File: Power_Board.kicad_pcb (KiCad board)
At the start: 2 copper layers, 48.3 x 24.1 mm, 7 parts, among them J1 Input Power (12 V), J2 Output Power (5V), SW1 SW_SPST, U1 NSR003A0X

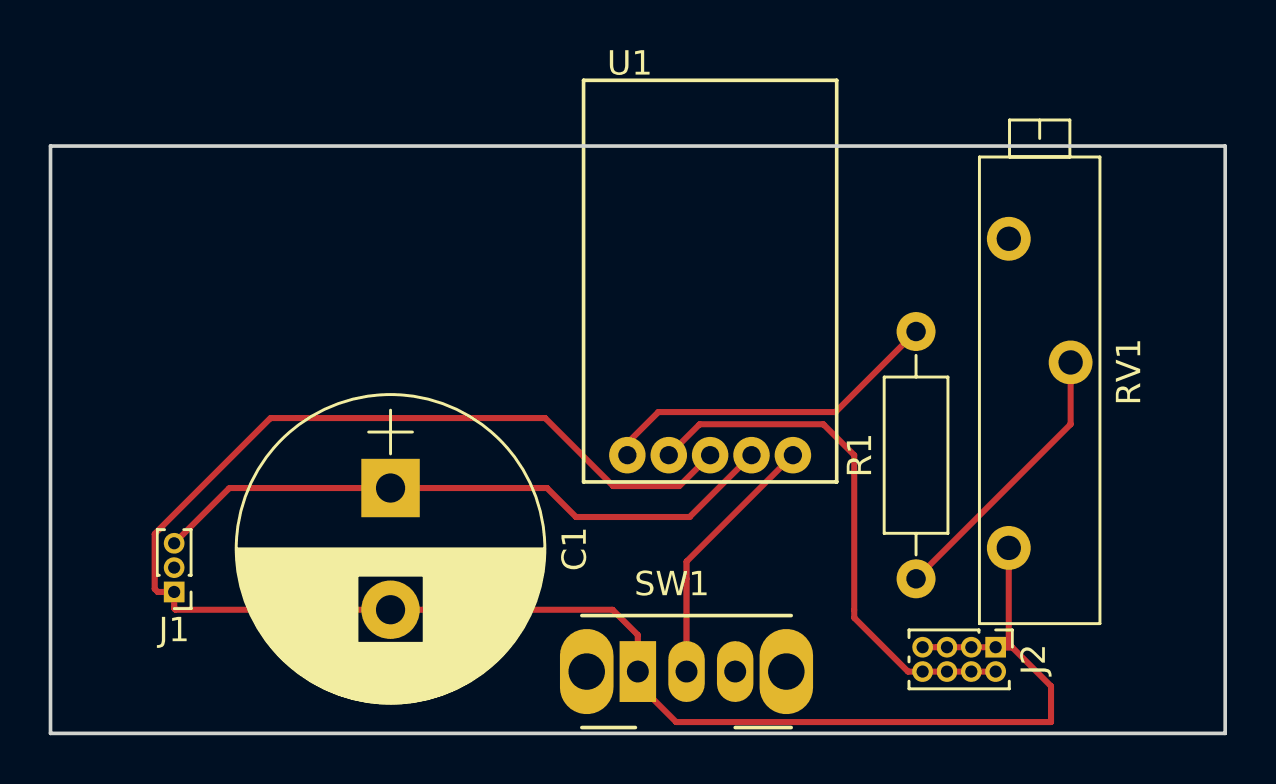
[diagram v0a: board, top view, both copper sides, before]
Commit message: Updated design, added backplane
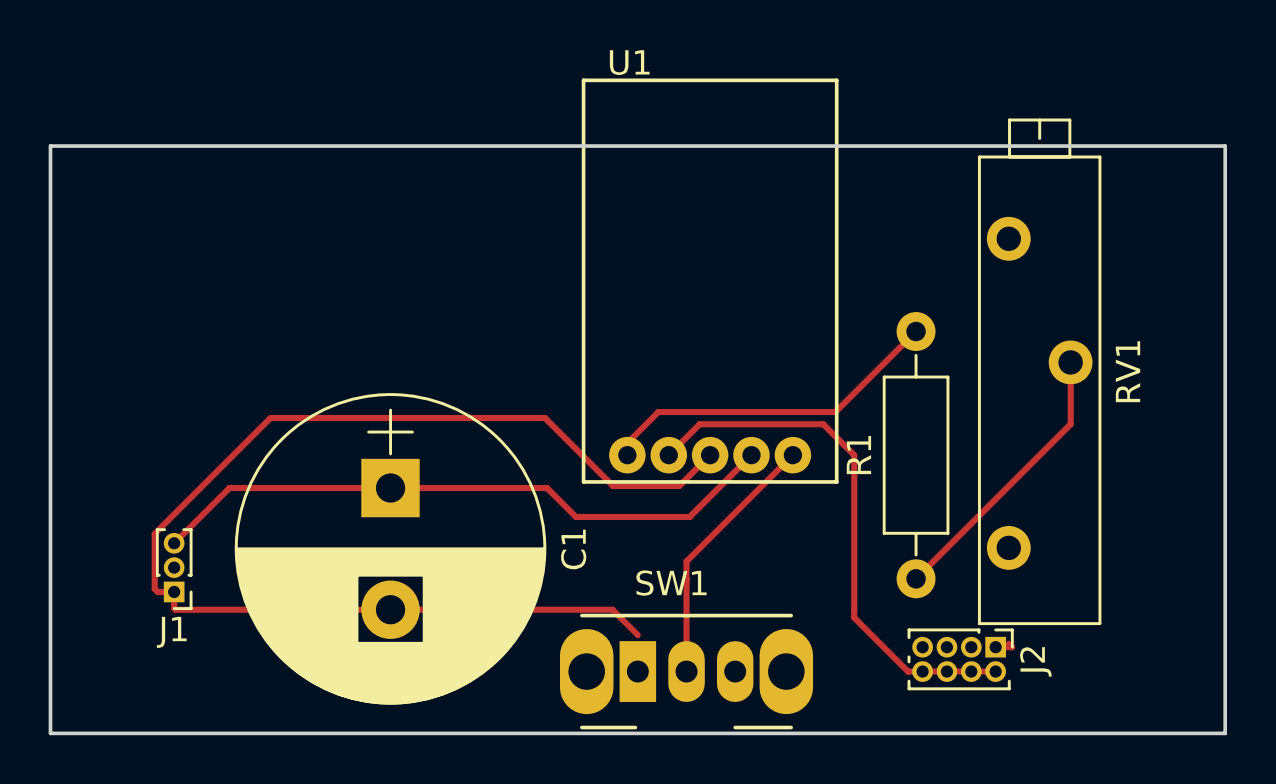
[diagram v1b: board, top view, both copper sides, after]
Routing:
- net Net-(C1-Pad2): track 81.6 -> 50.6 mm
- added copper zone on B.Cu, net (none)
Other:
- net class Default: clearance 0.25 -> 0.2
- rule trace_clearance: 0.25 -> 0.2
- rule trace_min: 0.25 -> 0.2
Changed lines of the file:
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@@
   (general
     (links 17)
-    (no_connects 13)
-    (area 100.625 88.335 150.79 128.155)
+    (no_connects 5)
+    (area 104.064999 97.714999 152.475001 121.995001)
     (thickness 1.6)
     (drawings 4)
-    (tracks 47)
+    (tracks 38)
     (zones 0)
     (modules 7)
@@
   (setup
     (last_trace_width 0.25)
-    (trace_clearance 0.25)
+    (trace_clearance 0.2)
     (zone_clearance 0.508)
     (zone_45_only no)
-    (trace_min 0.25)
+    (trace_min 0.2)
     (segment_width 0.2)
     (edge_width 0.15)
@@
   (net 8 "Net-(SW1-Pad2)")
   (net_class Default "This is the default net class."
-    (clearance 0.25)
+    (clearance 0.2)
     (trace_width 0.25)
     (via_dia 0.6)
@@
   (segment (start 118.11 116.84) (end 127.23 116.84) (width 0.25) (layer F.Cu) (net 2))
   (segment (start 127.23 116.84) (end 128.27 117.88) (width 0.25) (layer F.Cu) (net 2))
-  (segment (start 128.27 117.88) (end 128.27 119.38) (width 0.25) (layer F.Cu) (net 2))
   (segment (start 124.46 108.964999) (end 114.3 108.964999) (width 0.25) (layer F.Cu) (net 2))
   (segment (start 113.180999 108.964999) (end 114.3 108.964999) (width 0.25) (layer F.Cu) (net 2))
@@
   (segment (start 131.24 110.49) (end 129.97 111.76) (width 0.25) (layer F.Cu) (net 2))
   (segment (start 127.255001 111.76) (end 124.46 108.964999) (width 0.25) (layer F.Cu) (net 2))
-  (segment (start 143.51 114.3) (end 143.51 118.245) (width 0.25) (layer F.Cu) (net 2))
   (segment (start 143.51 118.245) (end 143.645 118.38) (width 0.25) (layer F.Cu) (net 2))
   (segment (start 143.645 118.38) (end 142.97 118.38) (width 0.25) (layer F.Cu) (net 2))
-  (segment (start 145.24499 121.45501) (end 145.24499 119.97999) (width 0.25) (layer F.Cu) (net 2))
-  (segment (start 140.57104 118.38) (end 139.97 118.38) (width 0.25) (layer F.Cu) (net 2))
-  (segment (start 145.24499 119.97999) (end 143.645 118.38) (width 0.25) (layer F.Cu) (net 2))
-  (segment (start 143.645 118.38) (end 140.57104 118.38) (width 0.25) (layer F.Cu) (net 2))
-  (segment (start 128.27 119.38) (end 128.27 119.88) (width 0.25) (layer F.Cu) (net 2))
-  (segment (start 128.27 119.88) (end 129.84501 121.45501) (width 0.25) (layer F.Cu) (net 2))
-  (segment (start 129.84501 121.45501) (end 145.24499 121.45501) (width 0.25) (layer F.Cu) (net 2))
   (segment (start 137.16 116.84) (end 137.16 110.49) (width 0.25) (layer F.Cu) (net 4))
   (segment (start 135.89 109.22) (end 137.16 110.49) (width 0.25) (layer F.Cu) (net 4))
@@
   (segment (start 134.64 110.49) (end 130.27 114.86) (width 0.25) (layer F.Cu) (net 8))
   (segment (start 130.27 114.86) (end 130.27 115.57) (width 0.25) (layer F.Cu) (net 8))
+  (zone (net 0) (net_name "") (layer F.Cu) (hatch edge 0.508)
+    (connect_pads (clearance 0.508))
+    (min_thickness 0.254)
+    (keepout (tracks allowed) (vias not_allowed) (copperpour not_allowed))
+    (fill (arc_segments 16) (thermal_gap 0.508) (thermal_bridge_width 0.508))
+    (polygon
+      (pts
+        (xy 127 110.49) (xy 124.46 110.49) (xy 124.46 111.76) (xy 125.73 113.03) (xy 130.81 113.03)
+        (xy 130.81 110.49)
+      )
+    )
+  )
   (zone (net 2) (net_name "Net-(C1-Pad2)") (layer F.Cu) (hatch edge 0.508)
     (connect_pads (clearance 0.508))
     (min_thickness 0.254)
+    (fill yes (arc_segments 16) (thermal_gap 0.508) (thermal_bridge_width 0.508))
+    (polygon
+      (pts
+        (xy 104.14 97.79) (xy 152.4 97.79) (xy 152.4 121.92) (xy 104.14 121.92)
+      )
+    )
+  )
+  (zone (net 0) (net_name "") (layer B.Cu) (hatch edge 0.508)
+    (connect_pads (clearance 0.508))
+    (min_thickness 0.254)

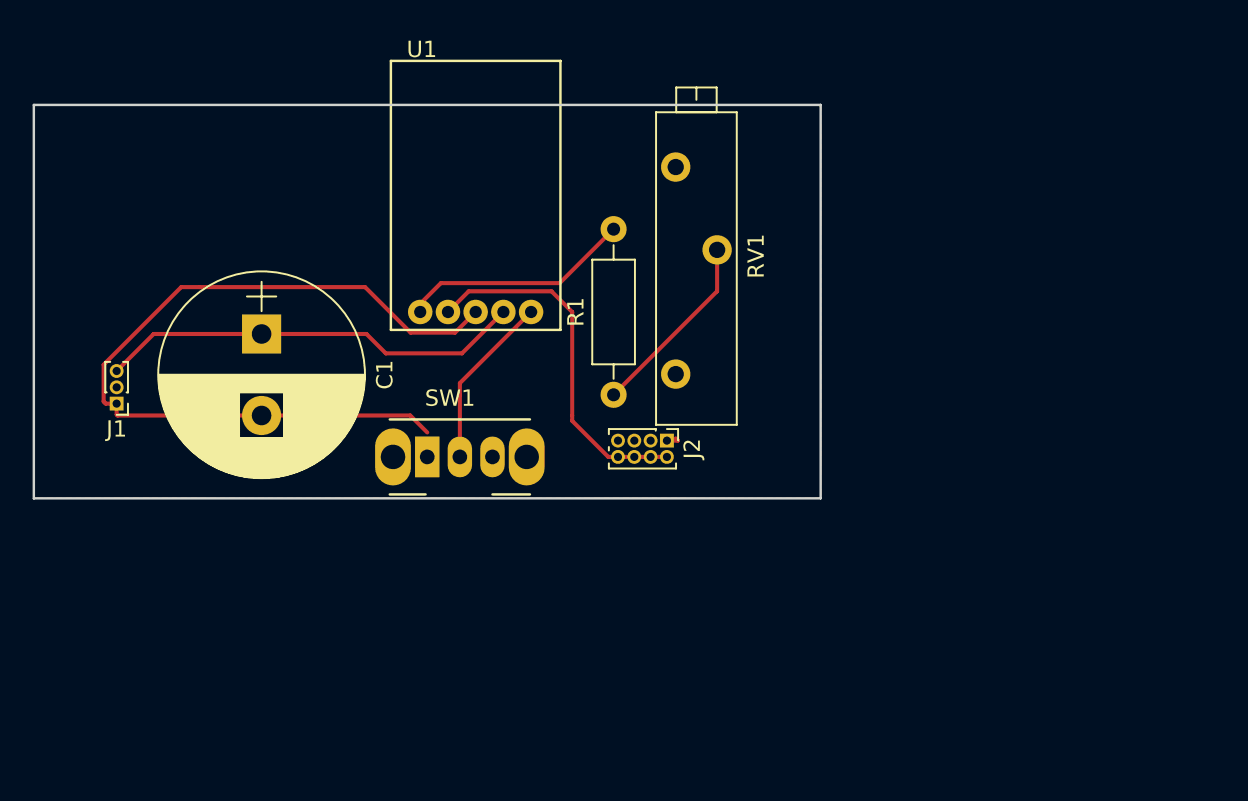
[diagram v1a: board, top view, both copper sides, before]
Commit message: Updated to version 2, corrected footprints
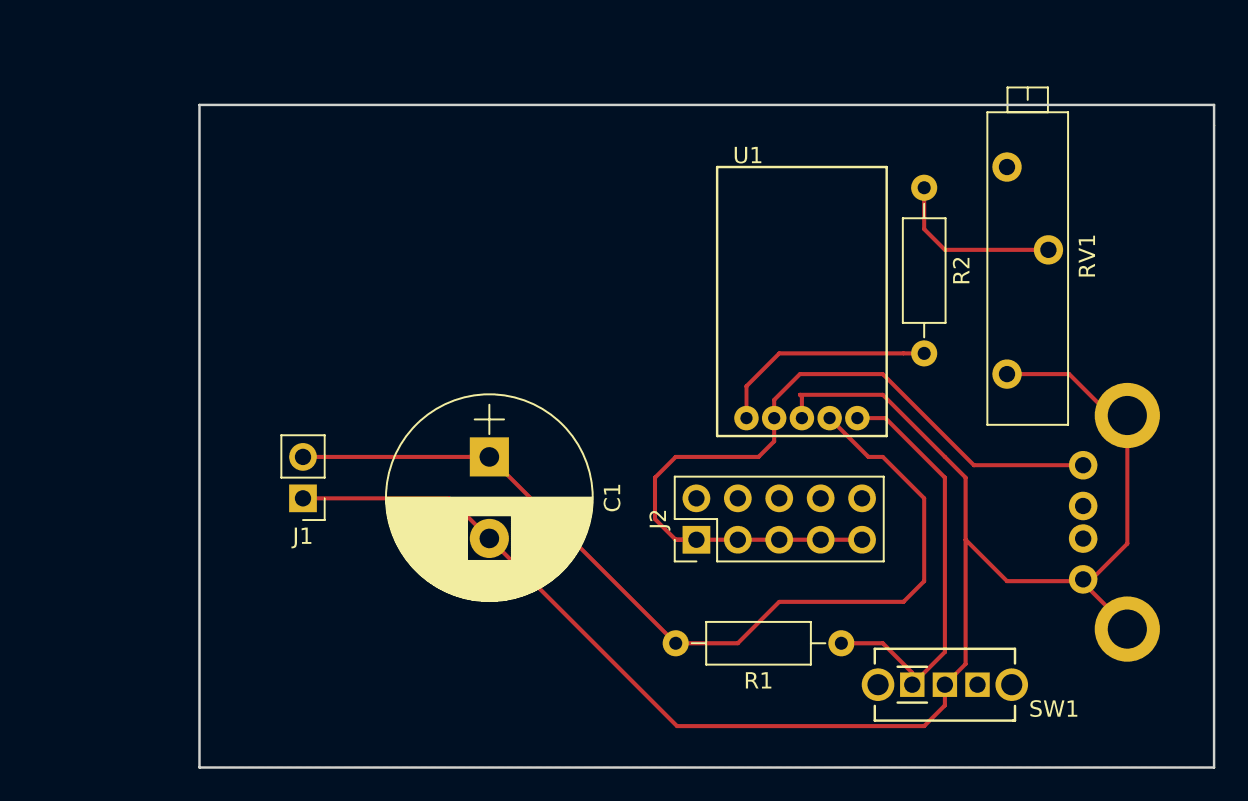
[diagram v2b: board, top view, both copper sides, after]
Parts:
- added J3: USB_A, NSR:UE27ACX4X0X, B.Cu at (167.6, 116.8)
- added R2: 240, Resistors_THT:R_Axial_DIN0207_L6.3mm_D2.5mm_P10.16mm_Horizontal, F.Cu at (158.8, 102.9)
- C1: value 100uF? -> 10u
- J1: value Input Power (12 V) -> Conn_01x02; footprint Pin_Headers:Pin_Header_Straight_1x03_Pitch1.00mm -> Pin_Headers:Pin_Header_Straight_1x02_Pitch2.54mm
- J2: value Output Power (5V) -> Conn_02x05; footprint Pin_Headers:Pin_Header_Straight_2x04_Pitch1.00mm -> Pin_Headers:Pin_Header_Straight_2x05_Pitch2.54mm
- R1: value 240 -> 10M
- SW1: footprint Buttons_Switches_THT:SW_CuK_OS102011MA1QN1_SPDT_Angled -> OS_Switches:OS102011MA1QN1
- U1: footprint NSR003A0X:NSR003A0X -> NSR:NSR003A0X
- moved SW1 34.7 mm to (160.0, 133.3)
- moved U1 21.0 mm to (146.1, 101.6)
- moved R1 20.7 mm to (153.7, 130.8), turned to 180 degrees
- moved RV1 20.3 mm to (163.8, 114.3)
- moved C1 15.9 mm to (132.1, 119.4)
- moved J1 12.8 mm to (120.7, 121.9)
- moved J2 6.34 mm to (144.8, 124.5), turned to 90 degrees
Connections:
- J1 pad 2: Net-(J1-Pad2) -> Net-(C1-Pad1)
- J2 pad 1: Net-(C1-Pad2) -> Net-(J2-Pad1)
- J2 pad 2: Net-(J2-Pad2) -> Net-(C1-Pad2)
- J2 pad 3: Net-(C1-Pad2) -> Net-(J2-Pad1)
- J2 pad 4: Net-(J2-Pad2) -> Net-(C1-Pad2)
- J2 pad 5: Net-(C1-Pad2) -> Net-(J2-Pad1)
- J2 pad 6: Net-(J2-Pad2) -> Net-(C1-Pad2)
- J2 pad 7: Net-(C1-Pad2) -> Net-(J2-Pad1)
- J2 pad 8: Net-(J2-Pad2) -> Net-(C1-Pad2)
- R1 pad 2: Net-(R1-Pad2) -> Net-(C1-Pad1)
- RV1 pad 2: Net-(R1-Pad1) -> Net-(R2-Pad1)
- SW1 pad 1: Net-(C1-Pad2) -> Net-(R1-Pad1)
- SW1 pad 2: Net-(SW1-Pad2) -> Net-(C1-Pad2)
- U1 pad 1: Net-(SW1-Pad2) -> Net-(R1-Pad1)
- U1 pad 4: Net-(J2-Pad2) -> Net-(J2-Pad1)
- U1 pad 5: Net-(R1-Pad2) -> Net-(R2-Pad2)
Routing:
- net Net-(C1-Pad2): track 50.6 -> 106.5 mm
- net Net-(J2-Pad1): track 0.00 -> 49.7 mm
- net Net-(C1-Pad1): track 26.2 -> 57.3 mm
- net Net-(J2-Pad2): track 22.3 -> 0.00 mm
- net Net-(R1-Pad1): track 11.5 -> 26.2 mm
- net Net-(R1-Pad2): track 13.8 -> 0.00 mm
- net Net-(R2-Pad2): track 0.00 -> 13.7 mm
- net Net-(SW1-Pad2): track 10.7 -> 0.00 mm
- net Net-(R2-Pad1): track 0.00 -> 10.7 mm
- removed copper zone on B.Cu, net (none)
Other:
- board size 48.3 x 24.1 mm -> 62.2 x 40.6 mm

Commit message: Moved location for board, attempting production v1
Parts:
- moved R2 138.1 mm to (44.5, 180.3), turned to 180 degrees
- moved C1 132.6 mm to (17.8, 186.7)
- moved J1 132.6 mm to (6.35, 189.2)
- moved SW1 132.6 mm to (45.7, 200.7)
- moved U1 132.6 mm to (31.8, 168.9)
- moved J2 132.6 mm to (30.5, 191.8)
- moved J3 132.6 mm to (53.3, 184.2)
- moved R1 132.6 mm to (39.4, 198.1)
- moved RV1 132.3 mm to (45.7, 174.0), turned to 180 degrees
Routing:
- net Net-(R2-Pad2): track 13.7 -> 5.46 mm
- net Net-(C1-Pad2): track 106.5 -> 99.1 mm
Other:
- board size 62.2 x 40.6 mm -> 59.7 x 33 mm
